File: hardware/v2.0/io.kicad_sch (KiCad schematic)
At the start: 1 part, among them U1 ECP5U-25F-CABGA256

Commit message: Repo links update
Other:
- title: Icepi Zero -> GammaPi Zero
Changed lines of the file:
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@@
 	(paper "A4")
 	(title_block
-		(title "Icepi Zero")
-		(date "2026-01-17")
-		(rev "v2.1")
+		(title "GammaPi Zero")
+		(date "2026-01-25")
+		(rev "v2.3.2")
 		(company "Vadym Vikulin, Chengyin Yao (cheyao)")
-		(comment 1 "https://github.com/vikulin/icepi-zero")
+		(comment 1 "https://github.com/vikulin/gammapi-zero")
 		(comment 2 "License: Solderpad")
 		(comment 9 "OSHWA FR000026")

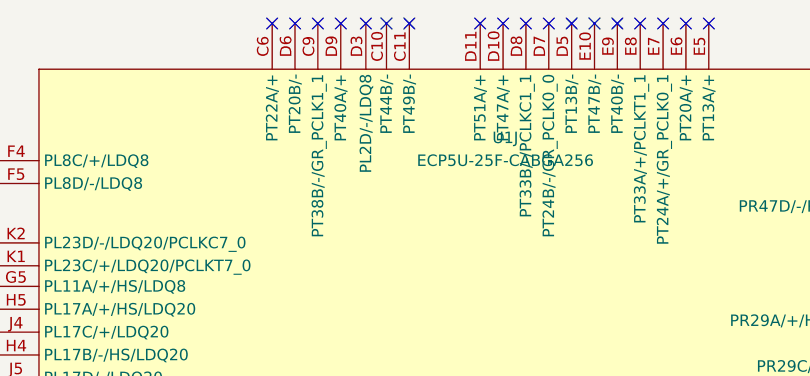
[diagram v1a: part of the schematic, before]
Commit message: Extra CS for SPI
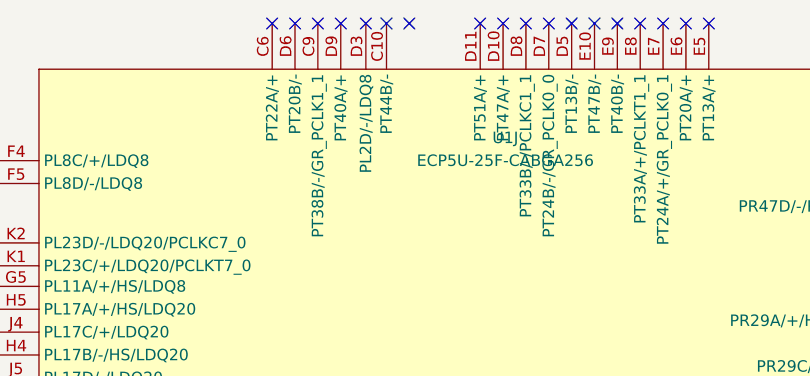
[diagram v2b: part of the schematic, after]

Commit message: DAC Vout
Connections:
- no-connect marks 70 -> 69
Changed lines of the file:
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@@
-	)
-	(no_connect
-		(at 144.526 50.8)
 	)
 	(no_connect
@@
 		(pin "C11"
 		)
+		(pin "E13"
+		)
+		(pin "E12"
+		)
+		(pin "D13"
+		)
 		(instances

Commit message: ERC pass
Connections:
- no-connect marks 69 -> 68
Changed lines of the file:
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@@
-	)
-	(no_connect
-		(at 98.298 124.46)
 	)
 	(no_connect
@@
 		(pin "R8"
 		)
-		(pin "E12"
-		)
 		(pin "L2"
 		)
 		(pin "R7"
 		)
-		(pin "E13"
-		)
 		(pin "F13"
 		)
@@
 		(pin "H6"
 		)
-		(pin "N6"
-		)
 		(pin "M5"
 		)
@@
 		(pin "C8"
 		)
-		(pin "D13"
-		)
 		(pin "G2"
